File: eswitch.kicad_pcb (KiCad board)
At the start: 4 copper layers, 181 x 57.5 mm, 153 parts, among them J1 Wuerth 691311400116, J2 +12V IN, J3 GND IN, J4 USB-C, J5 UART, SW1 RESET, SW2 BOOT, U1 BTS7004-1EPP, U10 ESP32-S3-WROOM-1-N8, U11 USBLC6-2SC6, U2 BTS7004-1EPP, U3 BTS7008-1EPP, U4 BTS7008-1EPP, U5 BTS7008-1EPP, U6 BTS7008-1EPP, U7 BTS7008-1EPP, U8 BTS7002-1EPP, U9 TPS54360B

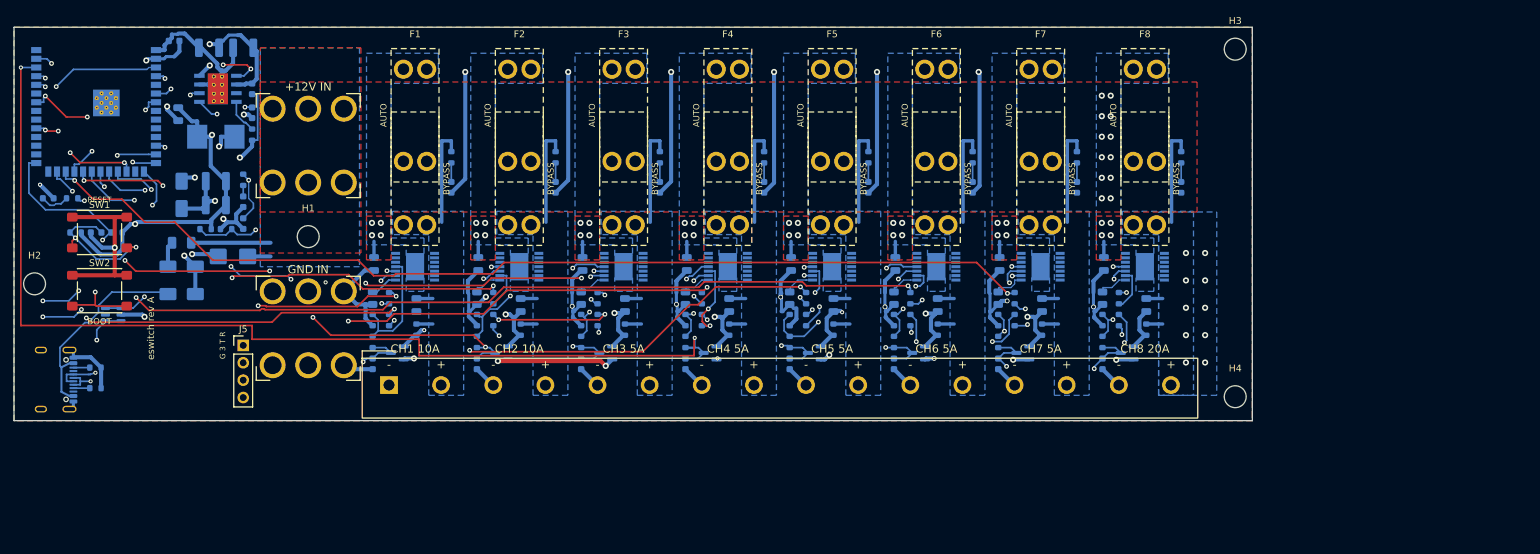
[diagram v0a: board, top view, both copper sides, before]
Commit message: Apply review corrections and circuit/fuse silk; hold fabrication
Add dated three-board DigiKey BOM for manual assembly, direct-entry outputs and higher-current input terminals. Mark each fuse with circuit identity and maximum fuse size. Preserve legacy fabrication files in a do-not-order archive and gate new outputs on release checks.

Not order-ready: eight signal connections remain after input terminal migration; native parity and electrical/layout/thermal findings are documented in docs/critical-review.md.
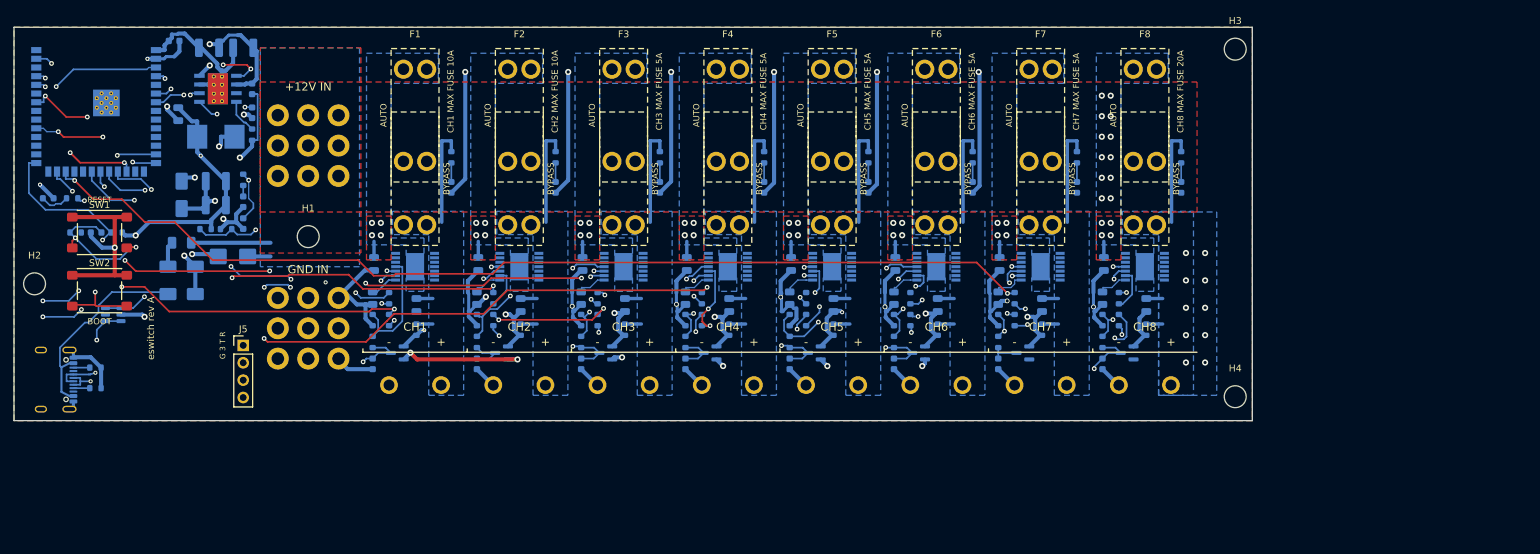
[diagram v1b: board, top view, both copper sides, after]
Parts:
- added J10: 691218410002, eswitch:TerminalBlock_1x02_P7.62mm_Wuerth_2184, F.Cu at (131.0, 52.3)
- added J11: 691218410002, eswitch:TerminalBlock_1x02_P7.62mm_Wuerth_2184, F.Cu at (146.2, 52.3)
- added J12: 691218410002, eswitch:TerminalBlock_1x02_P7.62mm_Wuerth_2184, F.Cu at (161.5, 52.3)
- added J6: 691218410002, eswitch:TerminalBlock_1x02_P7.62mm_Wuerth_2184, F.Cu at (70.0, 52.3)
- added J7: 691218410002, eswitch:TerminalBlock_1x02_P7.62mm_Wuerth_2184, F.Cu at (85.3, 52.3)
- added J8: 691218410002, eswitch:TerminalBlock_1x02_P7.62mm_Wuerth_2184, F.Cu at (100.5, 52.3)
- added J9: 691218410002, eswitch:TerminalBlock_1x02_P7.62mm_Wuerth_2184, F.Cu at (115.8, 52.3)
- C1, C2, C7, C8: footprint C_1210_3225Metric -> Capacitor_SMD:C_1210_3225Metric
- C10, C103, C11, C203, C3, C303, C4, C403, C5, C503, C6, C603, C703, C803: footprint C_0603_1608Metric -> Capacitor_SMD:C_0603_1608Metric
- C101, C102, C201, C202, C301, C302, C401, C402, C501, C502, C601, C602, C701, C702, C801, C802, C9: footprint C_0805_2012Metric -> Capacitor_SMD:C_0805_2012Metric
- D1, D2, D4: value SS36 -> B360A; footprint D_SMA -> Diode_SMD:D_SMA
- D101, D201, D301, D401, D501, D601, D701, D801: footprint SOT-23 -> Package_TO_SOT_SMD:SOT-23
- D102, D202, D302, D402, D5, D502, D602, D702, D802: footprint LED_0603_1608Metric -> LED_SMD:LED_0603_1608Metric
- D3: footprint D_SMB -> Diode_SMD:D_SMB
- F1, F2, F3, F4, F5, F6, F7, F8: footprint Fuseholder_ATO_3pos_Keystone_3557 -> eswitch:Fuseholder_ATO_3pos_Keystone_3557
- F9: footprint Fuse_1206_3216Metric -> Fuse:Fuse_1206_3216Metric
- H1, H2, H3, H4: footprint MountingHole_3.2mm_M3 -> MountingHole:MountingHole_3.2mm_M3
- J1: value Wuerth 691311400116 -> 691218410002; footprint TerminalBlock_1x16_P7.62mm_Wuerth_3114 -> eswitch:TerminalBlock_1x02_P7.62mm_Wuerth_2184
- J2, J3: footprint ScrewTerminal_Keystone_8196_10-32 -> eswitch:ScrewTerminal_Wuerth_74650195_M5
- J4: footprint USB_C_Receptacle_GCT_USB4105-xx-A_16P_TopMnt_Horizontal -> Connector_USB:USB_C_Receptacle_GCT_USB4105-xx-A_16P_TopMnt_Horizontal
- J5: footprint PinHeader_1x04_P2.54mm_Vertical -> Connector_PinHeader_2.54mm:PinHeader_1x04_P2.54mm_Vertical
- L1: footprint L_Bourns_SRP7028A_7.3x6.6mm -> Inductor_SMD:L_Bourns_SRP7028A_7.3x6.6mm
- R1, R101, R102, R104, R105, R106, R2, R201, R202, R204, R205, R206, R3, R301, R302, R304, R305, R306, R4, R401, R402, R404, R405, R406, R5, R501, R502, R504, R505, R506, R6, R601, R602, R604, R605, R606, R7, R701, R702, R704, R705, R706, R8, R801, R802, R804, R805, R806, R9: footprint R_0603_1608Metric -> Resistor_SMD:R_0603_1608Metric
- R103, R203, R303, R403, R503, R603, R703, R803: footprint R_0805_2012Metric -> Resistor_SMD:R_0805_2012Metric
- R107, R207, R307, R407, R507, R607, R707, R807: value 2.2k -> 10k; footprint R_0603_1608Metric -> Resistor_SMD:R_0603_1608Metric
- SW1, SW2: footprint SW_SPST_PTS645Sx43SMTR92 -> Button_Switch_SMD:SW_SPST_PTS645Sx43SMTR92
- U1, U2, U8: footprint Infineon_PG-TSDSO-14-22 -> Package_SO:Infineon_PG-TSDSO-14-22
- U10: footprint ESP32-S3-WROOM-1 -> RF_Module:ESP32-S3-WROOM-1
- U11: value USBLC6-2SC6 -> SRV05-4HTG-D; footprint SOT-23-6 -> Package_TO_SOT_SMD:SOT-23-6
- U3, U4, U5, U6, U7: value BTS7008-1EPP -> BTS7008-1EPR; footprint Infineon_PG-TSDSO-14-22 -> Package_SO:Infineon_PG-TSDSO-14-22
- U9: footprint TI_SO-PowerPAD-8_ThermalVias -> Package_SO:TI_SO-PowerPAD-8_ThermalVias
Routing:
- net IN6: track 150.4 -> 0.00 mm, vias 3 -> 0
- net IS4: track 154.2 -> 5.99 mm, vias 2 -> 0
- net IS7: track 149.2 -> 4.26 mm, vias 2 -> 0
- net IN5: track 123.1 -> 0.00 mm, vias 4 -> 0
- net IS2: track 69.4 -> 5.99 mm, vias 3 -> 0
- net +3V3: track 240.6 -> 197.0 mm, vias 11 -> 9
- net IN1: track 60.0 -> 67.0 mm, vias 3 -> 4
- net GND: track 406.7 -> 409.2 mm
- net IN4: track 104.2 -> 106.6 mm
- net DEN: track 219.2 -> 217.2 mm
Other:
- board text added: "CH1"
- board text added: "CH1 MAX FUSE 10A"
- board text added: "CH2"
- board text added: "CH2 MAX FUSE 10A"
- board text added: "CH3"
- board text added: "CH3 MAX FUSE 5A"
- board text added: "CH4"
- board text added: "CH4 MAX FUSE 5A"
- board text added: "CH5"
- board text added: "CH5 MAX FUSE 5A"
- board text added: "CH6"
- board text added: "CH6 MAX FUSE 5A"
- board text added: "CH7"
- board text added: "CH7 MAX FUSE 5A"
- board text added: "CH8"
- board text added: "CH8 MAX FUSE 20A"
- board text added: "LOGIC MAX 2A"
- board text removed: "CH1 10A"
- board text removed: "CH2 10A"
- board text removed: "CH3 5A"
- board text removed: "CH4 5A"
- board text removed: "CH5 5A"
- board text removed: "CH6 5A"
- board text removed: "CH7 5A"
- board text removed: "CH8 20A"

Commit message: Finish reviewed PCB routing and release checks
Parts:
- moved C10 2.60 mm to (23.4, 4.60), turned to 0 degrees
- moved C2 1.11 mm to (34.5, 3.48)
- moved C1 0.48 mm to (28.5, 3.48)
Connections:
- net BOOT renamed /BOOT
- net CC1 renamed /CC1
- net CC2 renamed /CC2
- net COMP renamed /COMP
- net COMPZ renamed /COMPZ
- net DEN renamed /DEN
- net DENR1 renamed /DENR1
- net DENR2 renamed /DENR2
- net DENR3 renamed /DENR3
- net DENR4 renamed /DENR4
- net DENR5 renamed /DENR5
- net DENR6 renamed /DENR6
- net DENR7 renamed /DENR7
- net DENR8 renamed /DENR8
- net EN renamed /EN
- net FB renamed /FB
- net IN1 renamed /IN1
- net IN2 renamed /IN2
- net IN3 renamed /IN3
- net IN4 renamed /IN4
- net IN5 renamed /IN5
- net IN6 renamed /IN6
- net IN7 renamed /IN7
- net IN8 renamed /IN8
- net INR1 renamed /INR1
- net INR2 renamed /INR2
- net INR3 renamed /INR3
- net INR4 renamed /INR4
- net INR5 renamed /INR5
- net INR6 renamed /INR6
- net INR7 renamed /INR7
- net INR8 renamed /INR8
- net IO0 renamed /IO0
- net IS1 renamed /IS1
- net IS2 renamed /IS2
- net IS3 renamed /IS3
- net IS4 renamed /IS4
- net IS5 renamed /IS5
- net IS6 renamed /IS6
- net IS7 renamed /IS7
- net IS8 renamed /IS8
- net ISP1 renamed /ISP1
- net ISP2 renamed /ISP2
- net ISP3 renamed /ISP3
- net ISP4 renamed /ISP4
- net ISP5 renamed /ISP5
- net ISP6 renamed /ISP6
- net ISP7 renamed /ISP7
- net ISP8 renamed /ISP8
- net LEDK1 renamed /LEDK1
- net LEDK2 renamed /LEDK2
- net LEDK3 renamed /LEDK3
- net LEDK4 renamed /LEDK4
- net LEDK5 renamed /LEDK5
- net LEDK6 renamed /LEDK6
- net LEDK7 renamed /LEDK7
- net LEDK8 renamed /LEDK8
- net LOAD1 renamed /LOAD1
- net LOAD2 renamed /LOAD2
- net LOAD3 renamed /LOAD3
- net LOAD4 renamed /LOAD4
- net LOAD5 renamed /LOAD5
- net LOAD6 renamed /LOAD6
- net LOAD7 renamed /LOAD7
- net LOAD8 renamed /LOAD8
- net RT renamed /RT
- net RXD0 renamed /RXD0
- net STAT renamed /STAT
- net STATK renamed /STATK
- net SW renamed /SW
- net TXD0 renamed /TXD0
- net UGND1 renamed /UGND1
- net UGND2 renamed /UGND2
- net UGND3 renamed /UGND3
- net UGND4 renamed /UGND4
- net UGND5 renamed /UGND5
- net UGND6 renamed /UGND6
- net UGND7 renamed /UGND7
- net UGND8 renamed /UGND8
- net USB_D+ renamed /USB_D+
- net USB_D- renamed /USB_D-
- net V12F renamed /V12F
- net VIN renamed /VIN
- net VS1 renamed /VS1
- net VS2 renamed /VS2
- net VS3 renamed /VS3
- net VS4 renamed /VS4
- net VS5 renamed /VS5
- net VS6 renamed /VS6
- net VS7 renamed /VS7
- net VS8 renamed /VS8
- J4 pad A8: unconnected-(J4-SBU1-PadA8) -> (no net)
- J4 pad B8: unconnected-(J4-SBU2-PadB8) -> (no net)
- U1 pad 11: unconnected-(U1-NC-Pad11) -> (no net)
- U1 pad 5: unconnected-(U1-NC-Pad5) -> (no net)
- U1 pad 6: unconnected-(U1-NC-Pad6) -> (no net)
- U1 pad 7: unconnected-(U1-NC-Pad7) -> (no net)
- U10 pad 10: unconnected-(U10-IO17-Pad10) -> (no net)
- U10 pad 11: unconnected-(U10-IO18-Pad11) -> (no net)
- U10 pad 16: unconnected-(U10-IO46-Pad16) -> (no net)
- U10 pad 26: unconnected-(U10-IO45-Pad26) -> (no net)
- U10 pad 28: unconnected-(U10-IO35-Pad28) -> (no net)
- U10 pad 29: unconnected-(U10-IO36-Pad29) -> (no net)
- U10 pad 30: unconnected-(U10-IO37-Pad30) -> (no net)
- U10 pad 32: unconnected-(U10-IO39-Pad32) -> (no net)
- U10 pad 33: unconnected-(U10-IO40-Pad33) -> (no net)
- U10 pad 35: unconnected-(U10-IO42-Pad35) -> (no net)
- U10 pad 8: unconnected-(U10-IO15-Pad8) -> (no net)
- U10 pad 9: unconnected-(U10-IO16-Pad9) -> (no net)
- U2 pad 11: unconnected-(U2-NC-Pad11) -> (no net)
- U2 pad 5: unconnected-(U2-NC-Pad5) -> (no net)
- U2 pad 6: unconnected-(U2-NC-Pad6) -> (no net)
- U2 pad 7: unconnected-(U2-NC-Pad7) -> (no net)
- U3 pad 11: unconnected-(U3-NC-Pad11) -> (no net)
- U3 pad 5: unconnected-(U3-NC-Pad5) -> (no net)
- U3 pad 6: unconnected-(U3-NC-Pad6) -> (no net)
- U3 pad 7: unconnected-(U3-NC-Pad7) -> (no net)
- U4 pad 11: unconnected-(U4-NC-Pad11) -> (no net)
- U4 pad 5: unconnected-(U4-NC-Pad5) -> (no net)
- U4 pad 6: unconnected-(U4-NC-Pad6) -> (no net)
- U4 pad 7: unconnected-(U4-NC-Pad7) -> (no net)
- U5 pad 11: unconnected-(U5-NC-Pad11) -> (no net)
- U5 pad 5: unconnected-(U5-NC-Pad5) -> (no net)
- U5 pad 6: unconnected-(U5-NC-Pad6) -> (no net)
- U5 pad 7: unconnected-(U5-NC-Pad7) -> (no net)
- U6 pad 11: unconnected-(U6-NC-Pad11) -> (no net)
- U6 pad 5: unconnected-(U6-NC-Pad5) -> (no net)
- U6 pad 6: unconnected-(U6-NC-Pad6) -> (no net)
- U6 pad 7: unconnected-(U6-NC-Pad7) -> (no net)
- U7 pad 11: unconnected-(U7-NC-Pad11) -> (no net)
- U7 pad 5: unconnected-(U7-NC-Pad5) -> (no net)
- U7 pad 6: unconnected-(U7-NC-Pad6) -> (no net)
- U7 pad 7: unconnected-(U7-NC-Pad7) -> (no net)
- U8 pad 11: unconnected-(U8-NC-Pad11) -> (no net)
- U8 pad 5: unconnected-(U8-NC-Pad5) -> (no net)
- U8 pad 6: unconnected-(U8-NC-Pad6) -> (no net)
- U8 pad 7: unconnected-(U8-NC-Pad7) -> (no net)
- U9 pad 3: unconnected-(U9-EN-Pad3) -> (no net)
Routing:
- net /IS7: track 4.26 -> 165.0 mm, vias 0 -> 6
- net /IN6: track 0.00 -> 152.6 mm, vias 0 -> 4
- net /IN5: track 0.00 -> 147.0 mm, vias 0 -> 5
- net /IS4: track 5.99 -> 145.5 mm, vias 0 -> 2
- net /IS2: track 5.99 -> 85.6 mm, vias 0 -> 2
- net +3V3: track 197.0 -> 237.9 mm, vias 9 -> 11
- net GND: track 409.2 -> 390.1 mm
- net /VIN: track 66.1 -> 73.9 mm, vias 2 -> 3
